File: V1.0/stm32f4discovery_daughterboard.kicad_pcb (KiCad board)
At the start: 2 copper layers, 99.9 x 70 mm, 142 parts, among them P1 CONN_25X2, P2 CONN_25X2, T1 BC547

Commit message: small changes
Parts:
- added VAL: paparazzi_35mm_back, paparazzi_35mm_back, F.Cu at (163.6, 116.1)
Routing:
- net 5V: track 74.1 -> 63.2 mm, vias 6 -> 13
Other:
- net class Default: via_dia 0.889 -> 0.7493; via_drill 0.635 -> 0.50038
- rule pad_to_mask_clearance: 0 -> 0.1016
- rule via_min_drill: 0.508 -> 0.50038
- rule via_min_size: 0.50038 -> 0.7493
- board text added: "Paparazzi"
- board text added: "The Free Autopilot"

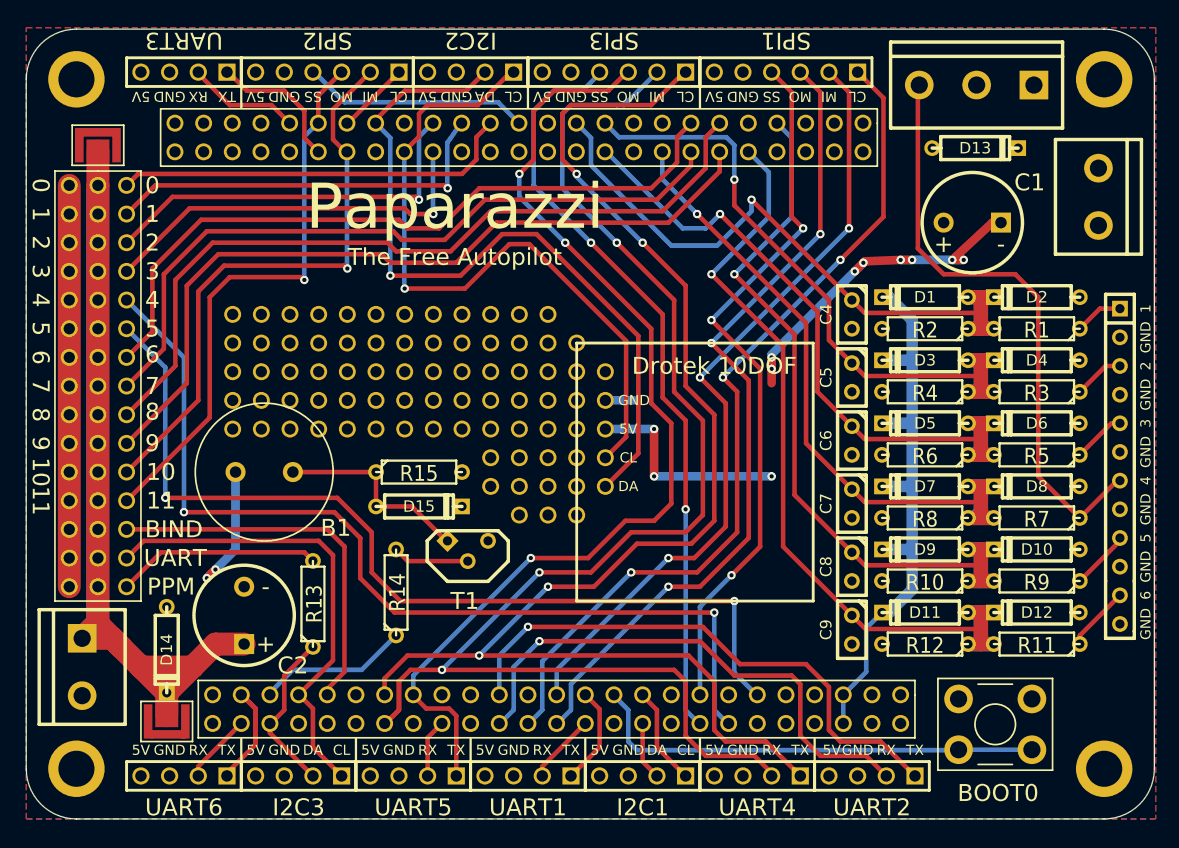
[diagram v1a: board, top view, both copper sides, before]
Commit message: added filter caps on input
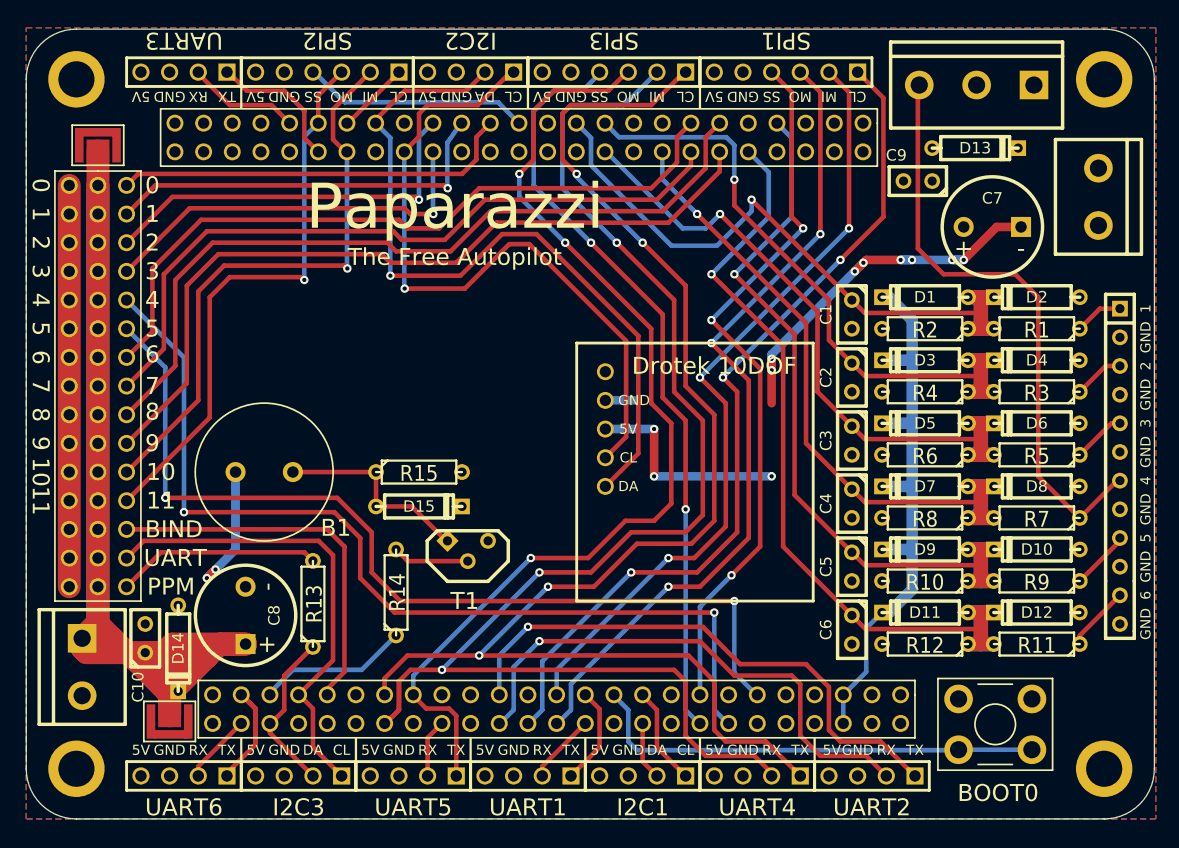
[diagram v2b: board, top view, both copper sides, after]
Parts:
- removed VAL: paparazzi_35mm_back, paparazzi_35mm_back
- removed thtpin (x75): VAL**, thtpin
- added C10: 100n, C1, F.Cu at (104.0, 127.8)
- added C3: 100n, C1, F.Cu at (166.6, 110.2)
- C1, C2: value CAPAPOL -> 100n; footprint C2V8 -> C1
- C7, C8: value 100n -> CAPAPOL; footprint C1 -> C2V8
- moved C2 57.8 mm to (166.6, 104.6), turned to 270 degrees
- moved C8 53.9 mm to (112.9, 125.7), turned to 90 degrees
- moved C9 40.2 mm to (172.5, 87.2), turned to 180 degrees
- moved C7 27.5 mm to (179.1, 91.3), turned to 180 degrees
- moved C5 16.8 mm to (166.6, 121.4)
- moved C4 16.8 mm to (166.6, 115.8)
- moved C6 16.8 mm to (166.6, 127.0)
- moved C1 13.4 mm to (166.6, 99.1), turned to 270 degrees
- moved D14 1.02 mm to (106.9, 128.7)
- moved JP1 0.25 mm to (106.2, 134.6)
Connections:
- C1 pad 1: 5V -> PB1
- C2 pad 1: PWM_VIN -> PC5
- C4 pad 1: PB1 -> PA4
- C5 pad 1: PC5 -> PC1
- C6 pad 1: PC4 -> PC2
- C7 pad 1: PA4 -> 5V
- C8 pad 1: PC1 -> PWM_VIN
- C9 pad 1: PC2 -> 5V
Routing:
- net PWM_VIN: track 112.3 -> 134.6 mm
- net 5V: track 63.2 -> 66.1 mm
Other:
- board text removed: "C1"
- board text removed: "C2"

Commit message: final v1.0
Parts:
- added thtpin: VAL**, thtpin, F.Cu at (142.2, 104.1)
- added thtpin: VAL**, thtpin, F.Cu at (137.2, 99.1)
- added thtpin: VAL**, thtpin, F.Cu at (137.2, 101.6)
- added thtpin: VAL**, thtpin, F.Cu at (139.7, 101.6)
- added thtpin: VAL**, thtpin, F.Cu at (142.2, 106.7)
- added thtpin: VAL**, thtpin, F.Cu at (139.7, 106.7)
- added thtpin: VAL**, thtpin, F.Cu at (137.2, 106.7)
- added thtpin: VAL**, thtpin, F.Cu at (134.6, 106.7)
- added thtpin: VAL**, thtpin, F.Cu at (132.1, 106.7)
- added thtpin: VAL**, thtpin, F.Cu at (132.1, 109.2)
- added thtpin: VAL**, thtpin, F.Cu at (134.6, 109.2)
- added thtpin: VAL**, thtpin, F.Cu at (139.7, 104.1)
- added thtpin: VAL**, thtpin, F.Cu at (137.2, 109.2)
- added thtpin: VAL**, thtpin, F.Cu at (139.7, 109.2)
- added thtpin: VAL**, thtpin, F.Cu at (142.2, 109.2)
- added thtpin: VAL**, thtpin, F.Cu at (134.6, 111.8)
- added thtpin: VAL**, thtpin, F.Cu at (137.2, 111.8)
- added thtpin: VAL**, thtpin, F.Cu at (139.7, 111.8)
- added thtpin: VAL**, thtpin, F.Cu at (142.2, 111.8)
- added thtpin: VAL**, thtpin, F.Cu at (142.2, 114.3)
- added thtpin: VAL**, thtpin, F.Cu at (142.2, 116.8)
- added thtpin: VAL**, thtpin, F.Cu at (139.7, 116.8)
- added thtpin: VAL**, thtpin, F.Cu at (137.2, 104.1)
- added thtpin: VAL**, thtpin, F.Cu at (137.2, 114.3)
- added thtpin: VAL**, thtpin, F.Cu at (137.2, 116.8)
- added thtpin: VAL**, thtpin, F.Cu at (134.6, 114.3)
- added thtpin: VAL**, thtpin, F.Cu at (139.7, 114.3)
- added thtpin: VAL**, thtpin, F.Cu at (129.5, 109.2)
- added thtpin: VAL**, thtpin, F.Cu at (127.0, 109.2)
- added thtpin: VAL**, thtpin, F.Cu at (124.5, 109.2)
- added thtpin: VAL**, thtpin, F.Cu at (121.9, 109.2)
- added thtpin: VAL**, thtpin, F.Cu at (119.4, 109.2)
- added thtpin: VAL**, thtpin, F.Cu at (116.8, 109.2)
- added thtpin: VAL**, thtpin, F.Cu at (134.6, 104.1)
- added thtpin: VAL**, thtpin, F.Cu at (114.3, 109.2)
- added thtpin: VAL**, thtpin, F.Cu at (111.8, 109.2)
- added thtpin: VAL**, thtpin, F.Cu at (111.8, 106.7)
- added thtpin: VAL**, thtpin, F.Cu at (111.8, 104.1)
- added thtpin: VAL**, thtpin, F.Cu at (111.8, 101.6)
- added thtpin: VAL**, thtpin, F.Cu at (111.8, 99.1)
- added thtpin: VAL**, thtpin, F.Cu at (114.3, 99.1)
- added thtpin: VAL**, thtpin, F.Cu at (116.8, 99.1)
- added thtpin: VAL**, thtpin, F.Cu at (119.4, 99.1)
- added thtpin: VAL**, thtpin, F.Cu at (121.9, 99.1)
- added thtpin: VAL**, thtpin, F.Cu at (132.1, 104.1)
- added thtpin: VAL**, thtpin, F.Cu at (124.5, 99.1)
- added thtpin: VAL**, thtpin, F.Cu at (127.0, 99.1)
- added thtpin: VAL**, thtpin, F.Cu at (129.5, 99.1)
- added thtpin: VAL**, thtpin, F.Cu at (139.7, 99.1)
- added thtpin: VAL**, thtpin, F.Cu at (142.2, 101.6)
- added thtpin: VAL**, thtpin, F.Cu at (129.5, 101.6)
- added thtpin: VAL**, thtpin, F.Cu at (129.5, 104.1)
- added thtpin: VAL**, thtpin, F.Cu at (129.5, 106.7)
- added thtpin: VAL**, thtpin, F.Cu at (127.0, 106.7)
- added thtpin: VAL**, thtpin, F.Cu at (124.5, 106.7)
- added thtpin: VAL**, thtpin, F.Cu at (132.1, 101.6)
- added thtpin: VAL**, thtpin, F.Cu at (121.9, 106.7)
- added thtpin: VAL**, thtpin, F.Cu at (119.4, 106.7)
- added thtpin: VAL**, thtpin, F.Cu at (116.8, 106.7)
- added thtpin: VAL**, thtpin, F.Cu at (114.3, 106.7)
- added thtpin: VAL**, thtpin, F.Cu at (114.3, 104.1)
- added thtpin: VAL**, thtpin, F.Cu at (114.3, 101.6)
- added thtpin: VAL**, thtpin, F.Cu at (116.8, 101.6)
- added thtpin: VAL**, thtpin, F.Cu at (119.4, 101.6)
- added thtpin: VAL**, thtpin, F.Cu at (121.9, 101.6)
- added thtpin: VAL**, thtpin, F.Cu at (124.5, 101.6)
- added thtpin: VAL**, thtpin, F.Cu at (132.1, 99.1)
- added thtpin: VAL**, thtpin, F.Cu at (127.0, 101.6)
- added thtpin: VAL**, thtpin, F.Cu at (127.0, 104.1)
- added thtpin: VAL**, thtpin, F.Cu at (124.5, 104.1)
- added thtpin: VAL**, thtpin, F.Cu at (121.9, 104.1)
- added thtpin: VAL**, thtpin, F.Cu at (119.4, 104.1)
- added thtpin: VAL**, thtpin, F.Cu at (116.8, 104.1)
- added thtpin: VAL**, thtpin, F.Cu at (134.6, 99.1)
- added thtpin: VAL**, thtpin, F.Cu at (134.6, 101.6)
- D1, D10, D11, D12, D13, D14, D15, D2, D3, D4, D5, D6, D7, D8, D9: footprint D3 -> do41_modified
- moved D13 1.02 mm to (178.6, 84.3)
- moved D14 0.28 mm to (106.8, 128.4)
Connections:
- BOOT0 pad 1: GND -> 3V
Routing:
- net GND: track 38.1 -> 103.6 mm, vias 0 -> 12
- net PWM_VIN: track 134.6 -> 179.7 mm
- net 3V: track 52.8 -> 69.9 mm
- net VDD: track 0.00 -> 2.54 mm
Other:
- board text added: "ADC4"
- board text added: "STM32F4 Discovery Daughterboard"
